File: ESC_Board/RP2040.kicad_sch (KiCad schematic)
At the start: 1 part, among them U1 RP2040

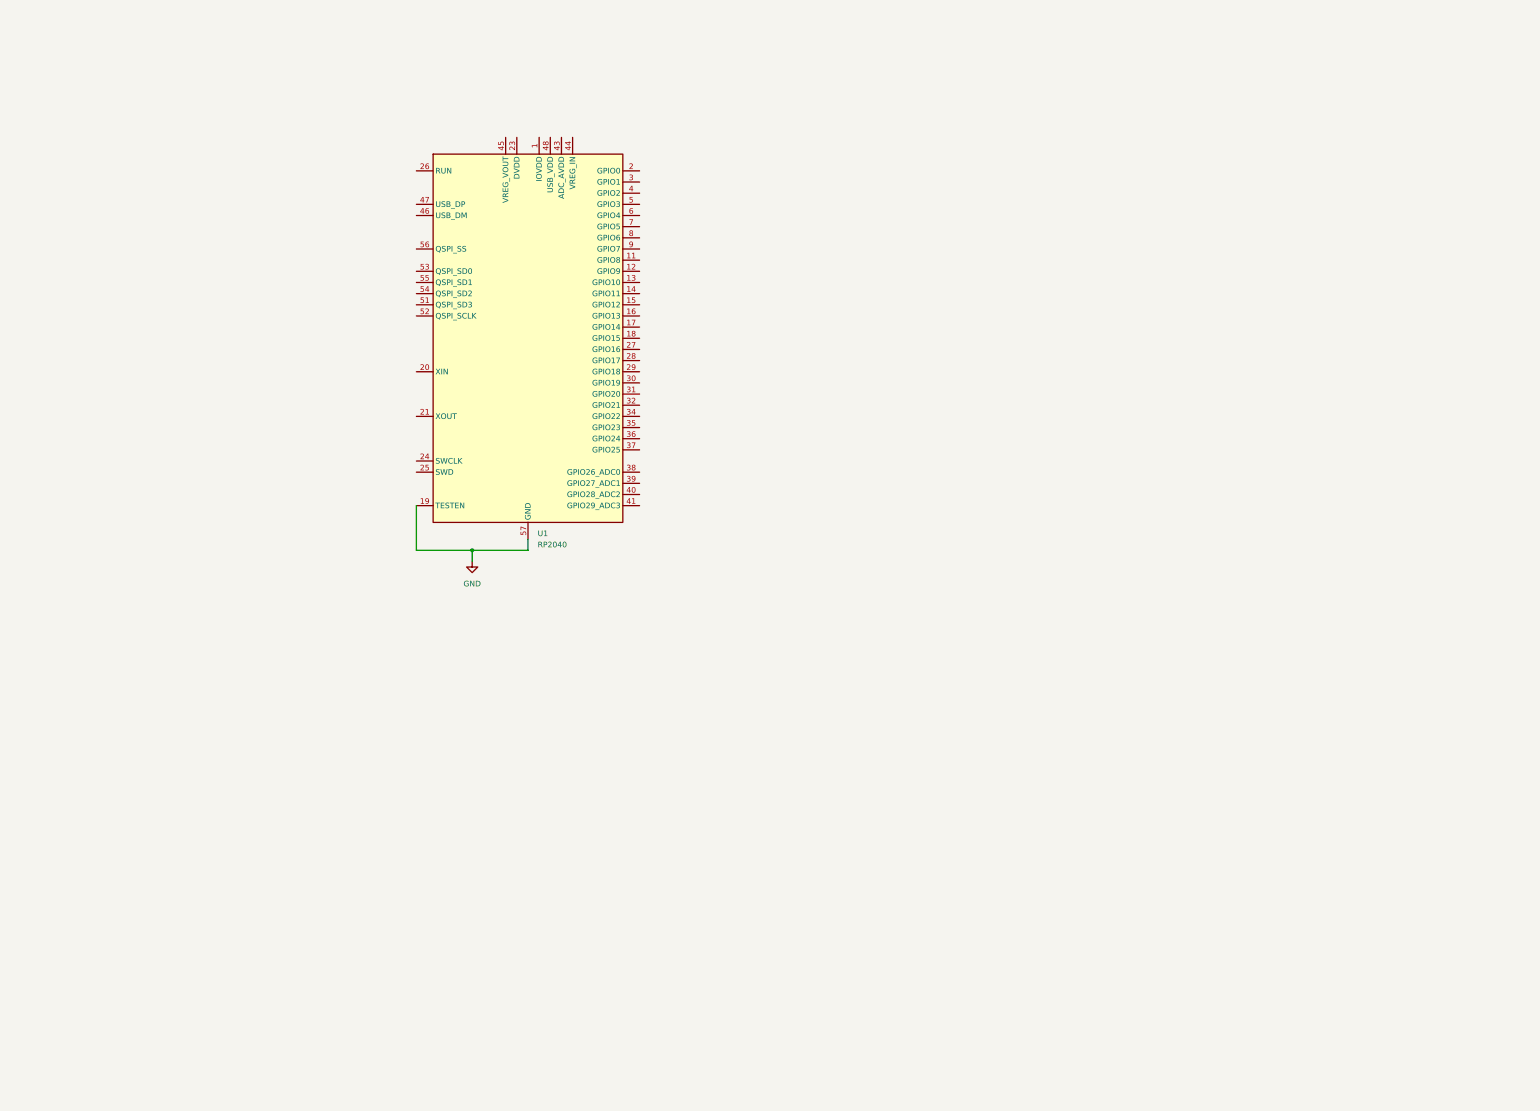
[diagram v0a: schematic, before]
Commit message: added basic rp2040 componets
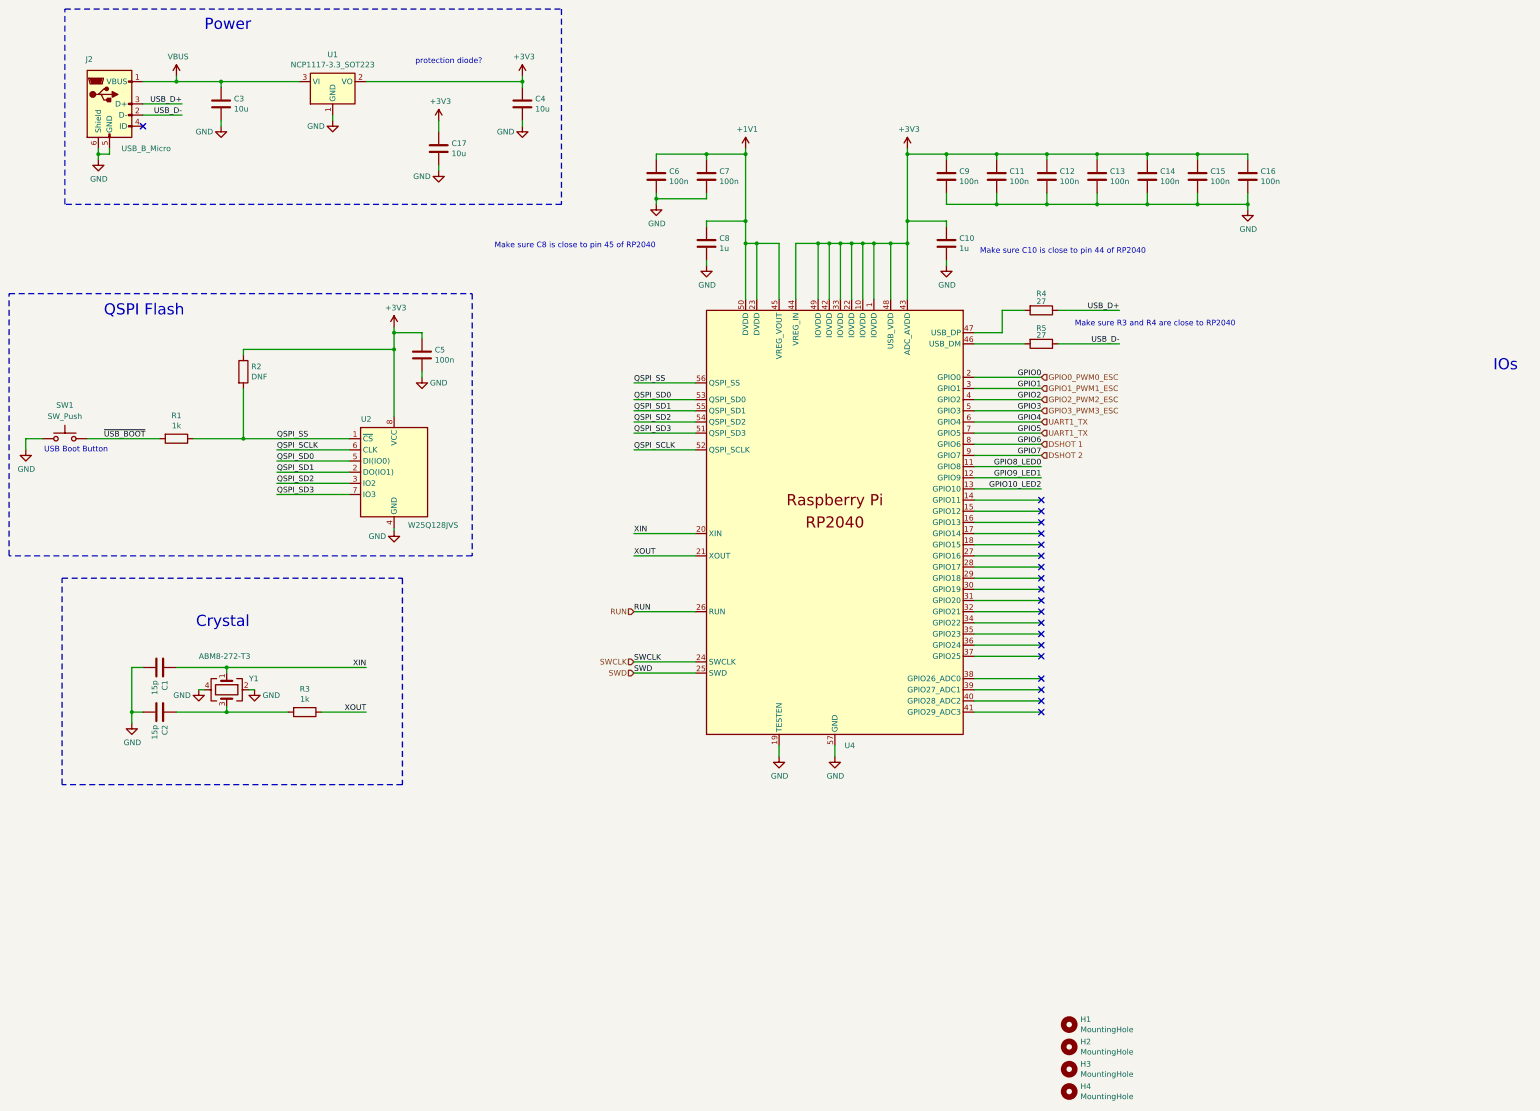
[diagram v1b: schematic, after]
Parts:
- removed U1: RP2040, Package_DFN_QFN:QFN-56-1EP_7x7mm_P0.4mm_EP3.2x3.2mm, symbol MCU_RaspberryPi:RP2040
- added C1, C2: 15p, Capacitor_SMD:C_0402_1005Metric, symbol Device:C
- added C10, C8: 1u, Capacitor_SMD:C_0402_1005Metric, symbol Device:C
- added C11, C12, C13, C14, C15, C16, C5, C6, C7, C9: 100n, Capacitor_SMD:C_0402_1005Metric, symbol Device:C
- added C17, C3, C4: 10u, Capacitor_SMD:C_0805_2012Metric, symbol Device:C
- added H1, H2, H3, H4: MountingHole, MountingHole:MountingHole_2.7mm_M2.5, symbol Mechanical:MountingHole
- added J2: USB_B_Micro, RP2040_minimal:USB_Micro-B_Amphenol_10103594-0001LF_Horizontal_modified, symbol Connector:USB_B_Micro
- added R1, R3: 1k, Resistor_SMD:R_0402_1005Metric, symbol Device:R
- added R2: DNF, Resistor_SMD:R_0402_1005Metric, symbol Device:R
- added R4, R5: 27, Resistor_SMD:R_0402_1005Metric, symbol Device:R
- added SW1: SW_Push, symbol Switch:SW_Push
- added U1: NCP1117-3.3_SOT223, Package_TO_SOT_SMD:SOT-223-3_TabPin2, symbol Regulator_Linear:NCP1117-3.3_SOT223
- added U2: W25Q128JVS, Package_SO:SOIC-8_5.23x5.23mm_P1.27mm, symbol Memory_Flash:W25Q128JVS
- added U4: ~, symbol RP_2040:RP2040
- added Y1: ABM8-272-T3, Crystal:Crystal_SMD_3225-4Pin_3.2x2.5mm, symbol Device:Crystal_GND24
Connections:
- net GND: now also C1.2, C10.2, C11.2, C12.2, C13.2, C14.2, C15.2, C16.2, C17.2, C2.2, C3.2, C4.2, C5.2, C6.2, C7.2, C8.2, C9.2, J2.5 (GND), J2.6 (Shield), SW1.1, U1.1 (GND), U2.4 (GND), U4.19 (TESTEN), U4.57 (GND), Y1.2, Y1.4
- new net: C2.1, R3.2, Y1.3
- new net: R5.2, U4.46 (USB_DM)
- new net: R4.2, U4.47 (USB_DP)
- new net +1V1: C6.1, C7.1, C8.1, U4.23 (DVDD), U4.45 (VREG_VOUT), U4.50 (DVDD)
- new net +3V3: C10.1, C11.1, C12.1, C13.1, C14.1, C15.1, C16.1, C17.1, C4.1, C5.1, C9.1, R2.1, U1.2 (VO), U2.8 (VCC), U4.1 (IOVDD), U4.10 (IOVDD), U4.22 (IOVDD), U4.33 (IOVDD), U4.42 (IOVDD), U4.43 (ADC_AVDD), U4.44 (VREG_IN), U4.48 (USB_VDD), U4.49 (IOVDD)
- new net DSHOT 1: U4.8 (GPIO6)
- new net DSHOT 2: U4.9 (GPIO7)
- new net GPIO0_PWM0_ESC: U4.2 (GPIO0)
- new net GPIO10_LED2: U4.13 (GPIO10)
- new net GPIO1_PWM1_ESC: U4.3 (GPIO1)
- new net GPIO2_PWM2_ESC: U4.4 (GPIO2)
- new net GPIO3_PWM3_ESC: U4.5 (GPIO3)
- new net GPIO8_LED0: U4.11 (GPIO8)
- new net GPIO9_LED1: U4.12 (GPIO9)
- new net QSPI_SCLK: U2.6 (CLK), U4.52 (QSPI_SCLK)
- new net QSPI_SD0: U2.5 (DI(IO0)), U4.53 (QSPI_SD0)
- new net QSPI_SD1: U2.2 (DO(IO1)), U4.55 (QSPI_SD1)
- new net QSPI_SD2: U2.3 (IO2), U4.54 (QSPI_SD2)
- new net QSPI_SD3: U2.7 (IO3), U4.51 (QSPI_SD3)
- new net QSPI_SS: R1.1, R2.2, U2.1 (~{CS}), U4.56 (QSPI_SS)
- new net RUN: U4.26 (RUN)
- new net SWCLK: U4.24 (SWCLK)
- new net SWD: U4.25 (SWD)
- new net UART1_TX: U4.6 (GPIO4), U4.7 (GPIO5)
- new net USB_D+: J2.3 (D+), R4.1
- new net USB_D-: J2.2 (D-), R5.1
- new net VBUS: C3.1, J2.1 (VBUS), U1.3 (VI)
- new net XIN: C1.1, U4.20 (XIN), Y1.1
- new net XOUT: R3.1, U4.21 (XOUT)
- new net ~{USB_BOOT}: R1.2, SW1.2
- no-connect marks 0 -> 20
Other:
- note added: "Crystal"
- note added: "IOs"
- note added: "Make sure C10 is close to pin 44 of RP2040"
- note added: "Make sure C8 is close to pin 45 of RP2040"
- note added: "Make sure R3 and R4 are close to RP2040"
- note added: "Power"
- note added: "QSPI Flash"
- note added: "USB Boot Button"
- note added: "protection diode?"
- company: (none) -> Cabrillo Robotics Club
- title: (none) -> ESC Board

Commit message: added esc interface pageand added test points to the rp2040 page
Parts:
- removed H1, H2, H3, H4: MountingHole, MountingHole:MountingHole_2.7mm_M2.5, symbol Mechanical:MountingHole
- added C18, C19: 100n, Capacitor_SMD:C_0402_1005Metric, symbol Device:C
- added D1: MBR120VLSFT1G, Diode_SMD:D_SOD-123, symbol Diode:MBR0520LT
- added D2, D3, D4: LED, symbol Device:LED
- added J1: Conn_01x03_Pin, symbol Connector:Conn_01x03_Pin
- added R6, R7, R8: 1K, symbol Device:R
- added R9: 10K, symbol Device:R
- added SW2: SW_Push, symbol Switch:SW_Push
- added TP1, TP2, TP3, TP4, TP5, TP6, TP7: TestPoint, symbol Connector:TestPoint
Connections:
- net +3V3: now also C18.1, C19.1, R9.1, TP7.1
- net DSHOT 1: now also TP5.1
- net DSHOT 2: now also TP6.1
- net GND: now also C18.2, C19.2, D2.1 (K), D3.1 (K), D4.1 (K), J1.3 (Pin_3), SW2.1
- net GPIO0_PWM0_ESC: now also TP1.1
- net GPIO1_PWM1_ESC: now also TP2.1
- net GPIO2_PWM2_ESC: now also TP3.1
- net GPIO3_PWM3_ESC: now also TP4.1
- net RUN: now also R9.2, SW2.2
- net SWCLK: now also J1.1 (Pin_1)
- net SWD: now also J1.2 (Pin_2)
- net UART1_TX: no longer U4.7 (GPIO5)
- net VBUS: now also D1.2 (A); no longer C3.1, U1.3 (VI)
- net GPIO25_LED0: now reaches U4.37 (GPIO25)
- net GPIO25_LED0: now also R6.1
- net GPIO10_LED2: no longer names the net of U4.13 (GPIO10)
- net GPIO8_LED0 renamed GPIO8_LED1
- net GPIO8_LED1: now also R7.1
- net GPIO9_LED1 renamed GPIO9_LED2
- net GPIO9_LED2: now also R8.1
- new net: D2.2 (A), R6.2
- new net: D4.2 (A), R8.2
- new net: D3.2 (A), R7.2
- new net 5V: C3.1, D1.1 (K), U1.3 (VI)
- new net UART1_RX: U4.7 (GPIO5)
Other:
- note added: "Close to ADC_AVDD"
- note added: "Debug Interface"
- note added: "Debug/ Testing Pins"
- note added: "Decoupling Capactors"
- note added: "Dshot Test Points"
- note added: "Each close to a DVDD pin"
- note added: "Each close to an IOVDD pin"
- note added: "GPIO Status LEDs"
- note added: "PWM Test Points"
- note added: "RESET Button"
- note added: "RP2040 Microcontroller"
- note removed: "IOs"
- moved on the sheet: C1, C10, C11, C12, C13, C14, C15, C16, C17, C2, C3, C4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

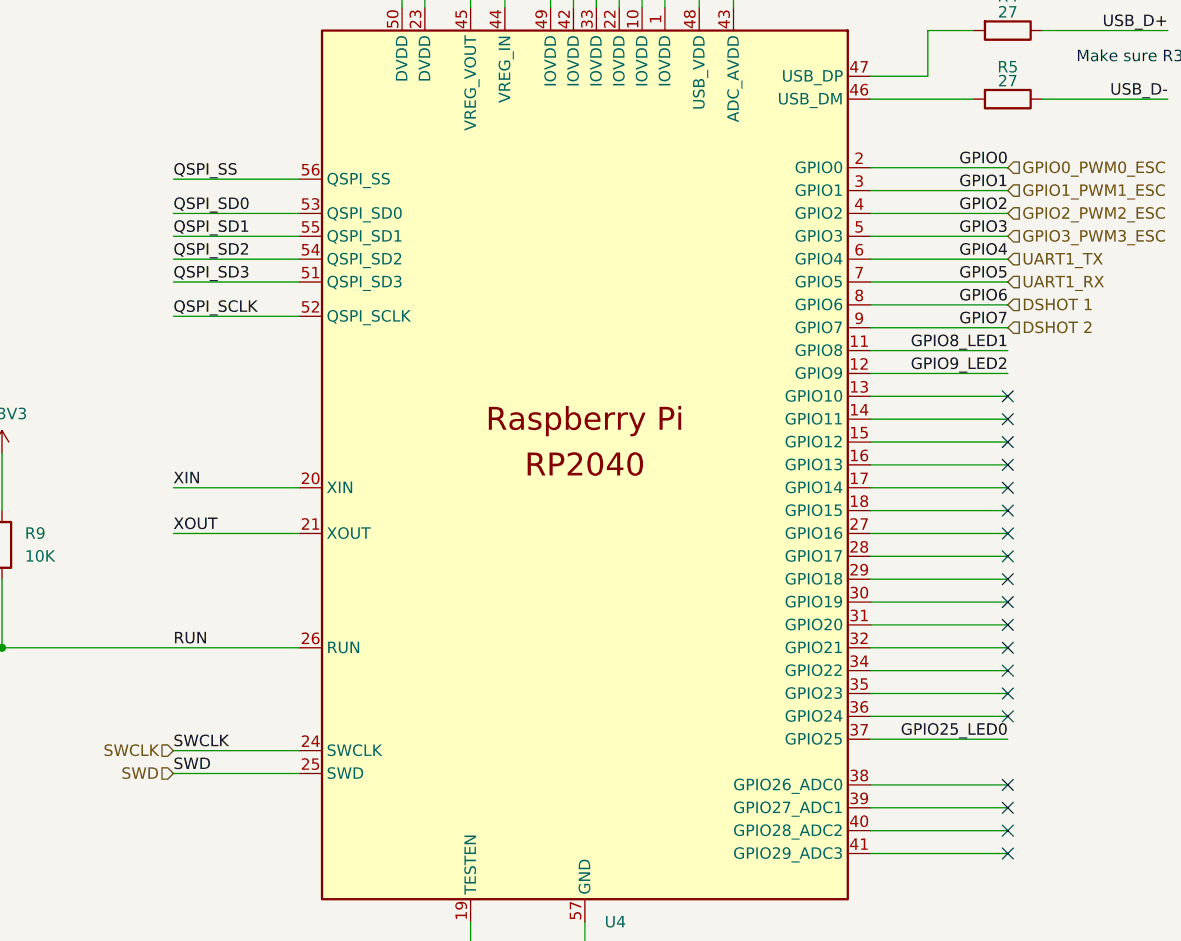
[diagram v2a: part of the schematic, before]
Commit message: schematic done, ready for review. need to think about how this will connect to the backplane
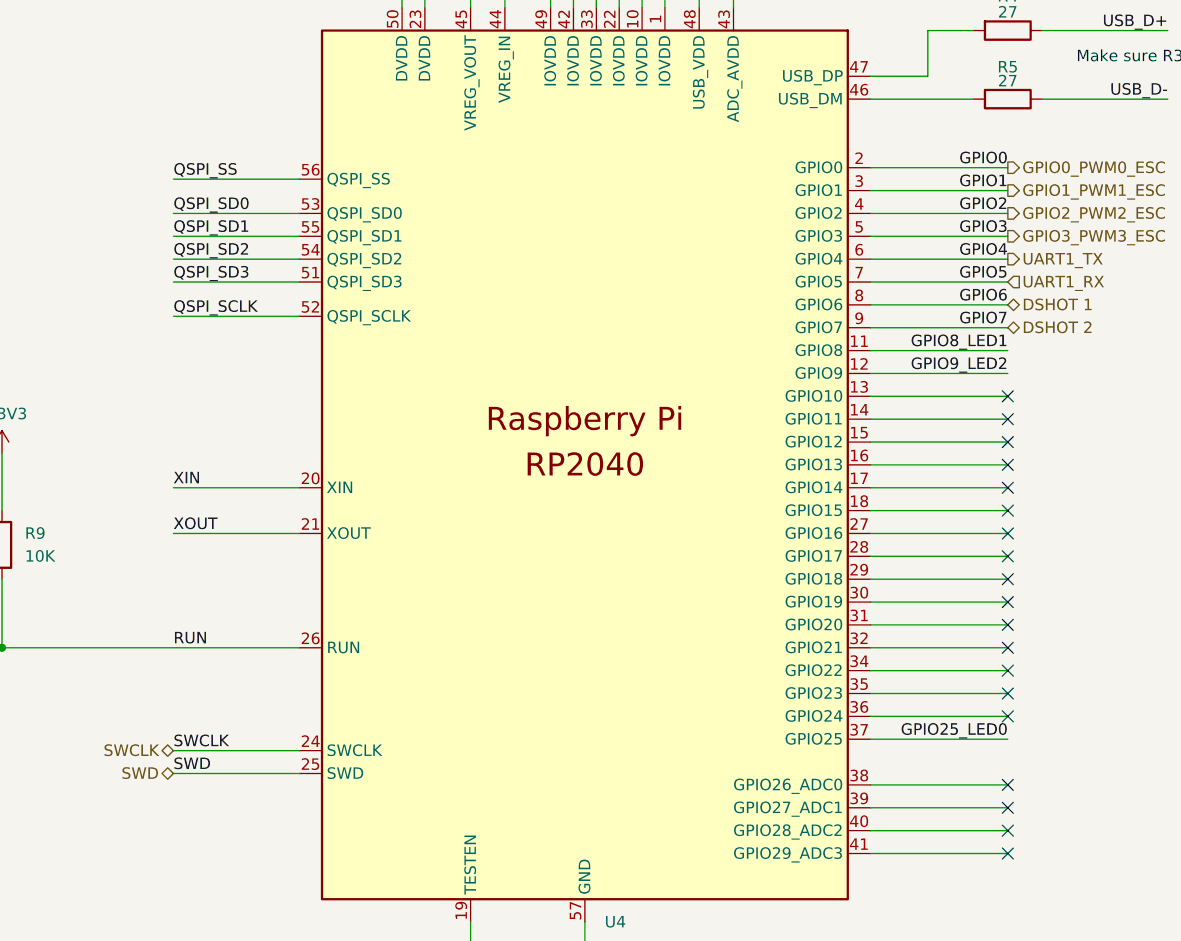
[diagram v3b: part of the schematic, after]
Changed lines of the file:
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@@
 	)
 	(hierarchical_label "GPIO2_PWM2_ESC"
-		(shape input)
+		(shape output)
 		(at 304.8 104.14 0)
 		(fields_autoplaced yes)
@@
 	)
 	(hierarchical_label "DSHOT 1"
-		(shape input)
+		(shape bidirectional)
 		(at 304.8 114.3 0)
 		(fields_autoplaced yes)
@@
 	)
 	(hierarchical_label "GPIO1_PWM1_ESC"
-		(shape input)
+		(shape output)
 		(at 304.8 101.6 0)
 		(fields_autoplaced yes)
@@
 	)
 	(hierarchical_label "UART1_TX"
-		(shape input)
+		(shape output)
 		(at 304.8 109.22 0)
 		(fields_autoplaced yes)
@@
 	)
 	(hierarchical_label "DSHOT 2"
-		(shape input)
+		(shape bidirectional)
 		(at 304.8 116.84 0)
 		(fields_autoplaced yes)
@@
 	)
 	(hierarchical_label "GPIO3_PWM3_ESC"
-		(shape input)
+		(shape output)
 		(at 304.8 106.68 0)
 		(fields_autoplaced yes)
@@
 	)
 	(hierarchical_label "SWCLK"
-		(shape input)
+		(shape bidirectional)
 		(at 212.09 163.83 180)
 		(fields_autoplaced yes)
@@
 	)
 	(hierarchical_label "SWD"
-		(shape input)
+		(shape bidirectional)
 		(at 212.09 166.37 180)
 		(fields_autoplaced yes)
@@
 	)
 	(hierarchical_label "GPIO0_PWM0_ESC"
-		(shape input)
+		(shape output)
 		(at 304.8 99.06 0)
 		(fields_autoplaced yes)

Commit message: esc board updated
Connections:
- net GPIO0_PWM0_ESC renamed GPIO0
- net GPIO1_PWM1_ESC renamed GPIO1
- net GPIO2_PWM2_ESC renamed GPIO2
- net GPIO3_PWM3_ESC renamed GPIO3
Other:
- note added: "Clean up this totaly fucked naming"
- company: Cabrillo Robotics Club -> Cabrillo Robotics
- title: ESC Board -> RP2040 MCU

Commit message: added more updates
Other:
- note removed: "Clean up this totaly fucked naming"
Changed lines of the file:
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@@
-		)
-	)
-	(text "Clean up this totaly fucked naming"
-		(exclude_from_sim no)
-		(at 324.612 120.65 0)
-		(effects
-			(font
-				(size 1.27 1.27)
-			)
 		)
 	)

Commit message: backup before heavy revtion
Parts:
- removed C1, C2: 15p, Capacitor_SMD:C_0402_1005Metric, symbol Device:C
- removed C5: 100n, Capacitor_SMD:C_0402_1005Metric, symbol Device:C
- removed R1, R3: 1k, Resistor_SMD:R_0402_1005Metric, symbol Device:R
- removed R2: DNF, Resistor_SMD:R_0402_1005Metric, symbol Device:R
- removed SW1: SW_Push, symbol Switch:SW_Push
- removed U2: W25Q128JVS, Package_SO:SOIC-8_5.23x5.23mm_P1.27mm, symbol Memory_Flash:W25Q128JVS
- removed Y1: ABM8-272-T3, Crystal:Crystal_SMD_3225-4Pin_3.2x2.5mm, symbol Device:Crystal_GND24
- added D7: MBR120VLSFT1G, Diode_SMD:D_SOD-123, symbol Diode:MBR0520LT
- added U3: Pico, RPi_Pico:RPi_Pico_SMD_TH, symbol MCU_RaspberryPi_and_Boards:Pico
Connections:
- net GND: now also U3.18 (GND), U3.23 (GND), U3.28 (GND), U3.3 (GND), U3.38 (GND), U3.42 (GND), U3.8 (GND)
- net SWCLK: now also U3.41 (SWCLK)
- net SWD: now also U3.43 (SWDIO)
- new net: D7.1 (K), U3.39 (VSYS)
- new net +5V: D7.2 (A)
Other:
- note added: "Pi Pico Microcontroller"
- note removed: "Crystal"
- note removed: "Decoupling Capactors"
- note removed: "QSPI Flash"
- note removed: "RP2040 Microcontroller"
- note removed: "USB Boot Button"
- moved on the sheet: C10, C11, C12, C13, C14, C15, C16, C17, C18, C19, C3, C4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
